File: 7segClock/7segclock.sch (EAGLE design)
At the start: 19 parts, among them J1 ICSP, J2 ZX62R-AB-5P, Q1 CSTNE16M0V530000R0, U1 ATMEGA328P-AU-TQFP32, U2 TM1640, U3 CP2104

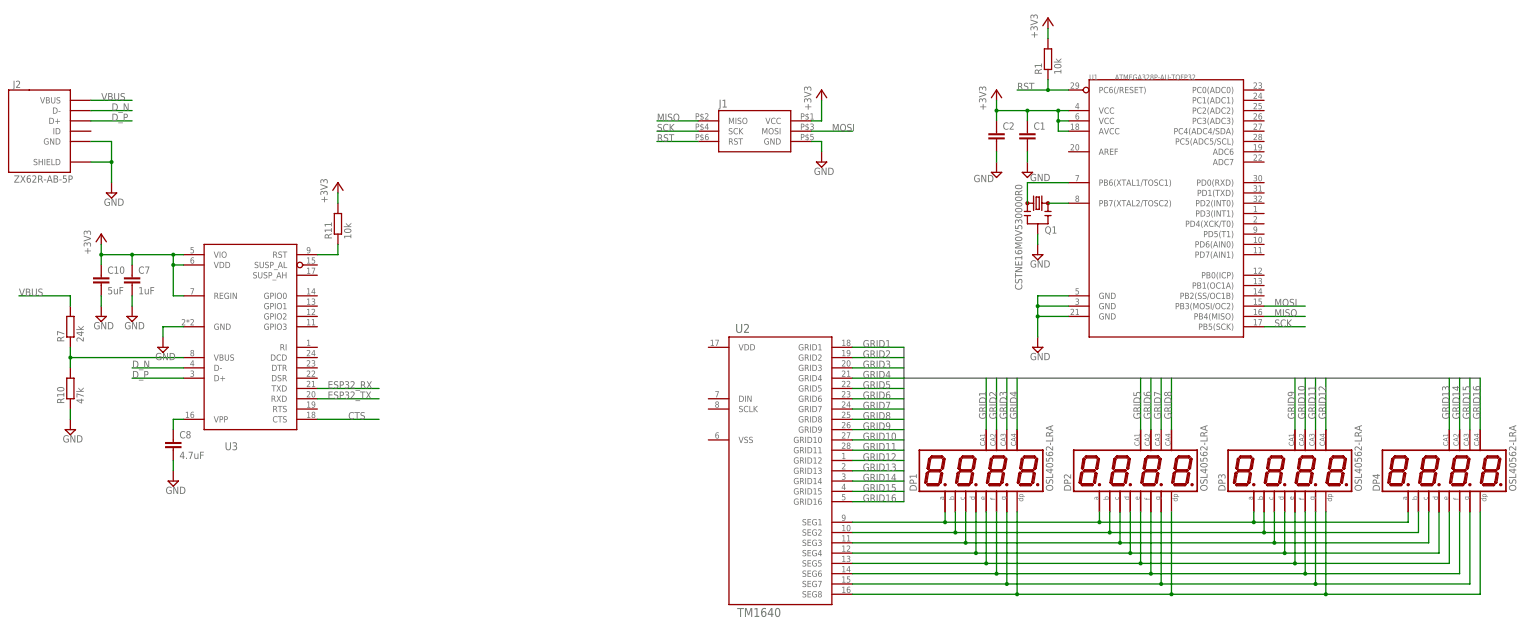
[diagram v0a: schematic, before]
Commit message: [add]add 7seg clokc before autoroute
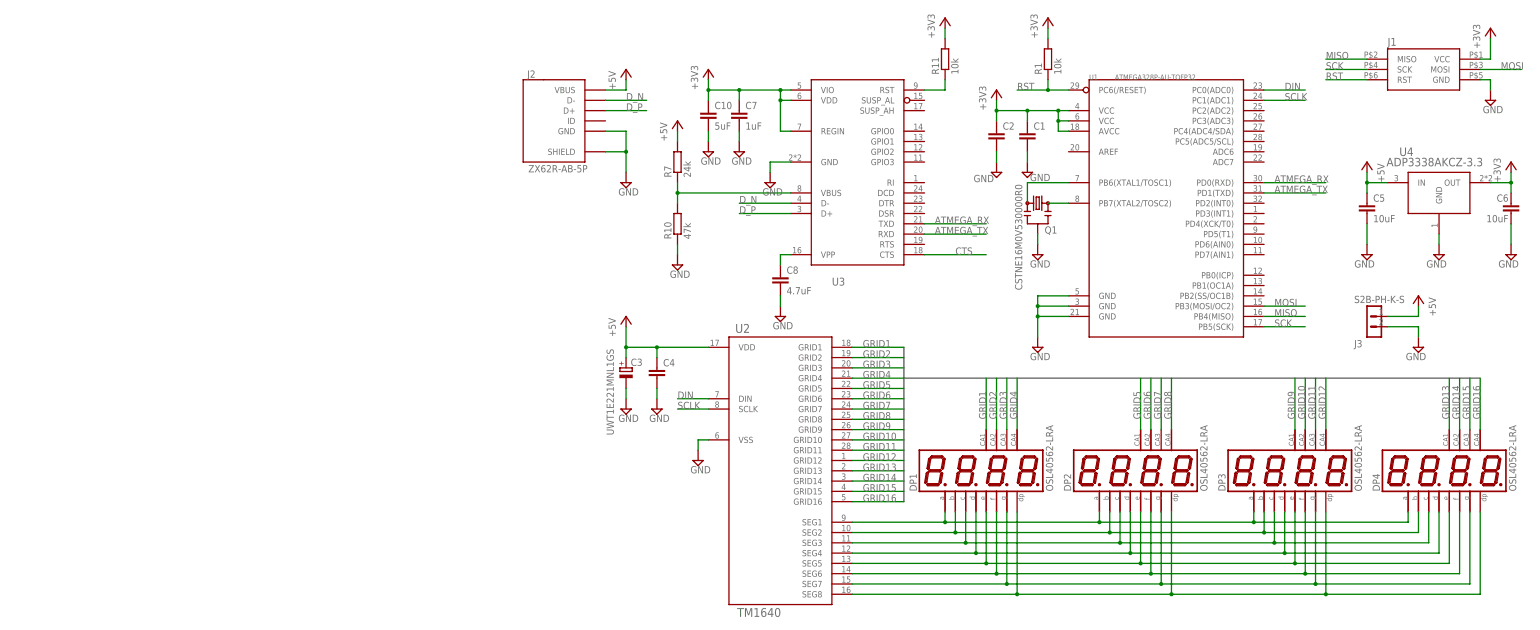
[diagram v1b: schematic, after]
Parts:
- added C3: UWT1E221MNL1GS, taki-library:UWT1E221MNL1GS
- added C4: (no value), taki-library:C-EUC0603
- added C5, C6: 10uF, taki-library:C-EUC0603
- added J3: S2B-PH-K-S, taki-library:S2B-PH-K-S
- added U4: ADP3338AKCZ-3.3, taki-library:ADP3338AKCZ-3.3
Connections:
- removed net ESP32_RX: U3.TXD
- removed net ESP32_TX: U3.RXD
- removed net VBUS: J2.VBUS, R7.2
- new net +5V: C3.+, C4.1, C5.1, J2.VBUS, J3.1, R7.2, U2.VDD, U4.IN
- new net ATMEGA_RX: U1.PD0(RXD), U3.TXD
- new net ATMEGA_TX: U1.PD1(TXD), U3.RXD
- new net DIN: U1.PC0(ADC0), U2.DIN
- new net SCLK: U1.PC1(ADC1), U2.SCLK
- net +3V3: now also C6.1, U4.OUT
- net GND: now also C3.-, C4.2, C5.2, C6.2, J3.2, U2.VSS, U4.GND
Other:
- moved on the sheet: C10, C7, C8, J1, J2, R10, R11, R7, U3

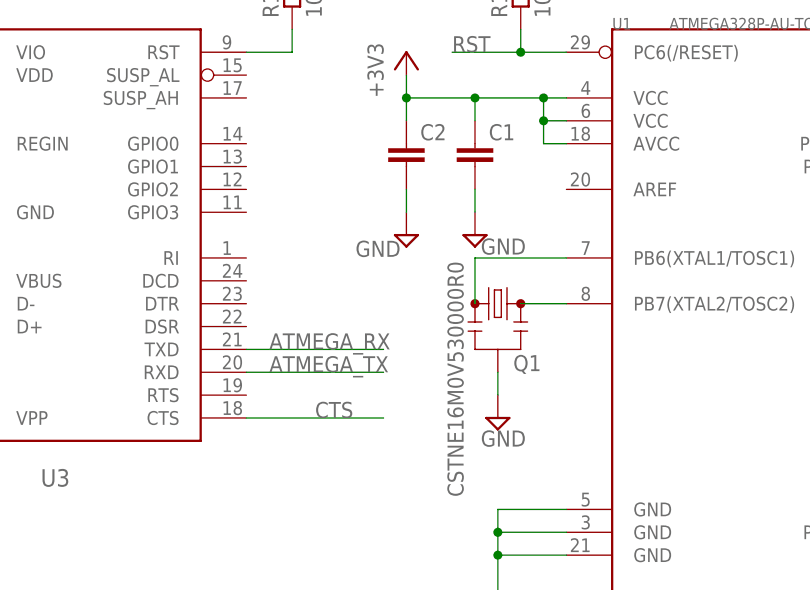
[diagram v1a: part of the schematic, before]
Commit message: [add]add gerver output of 7seg clokc
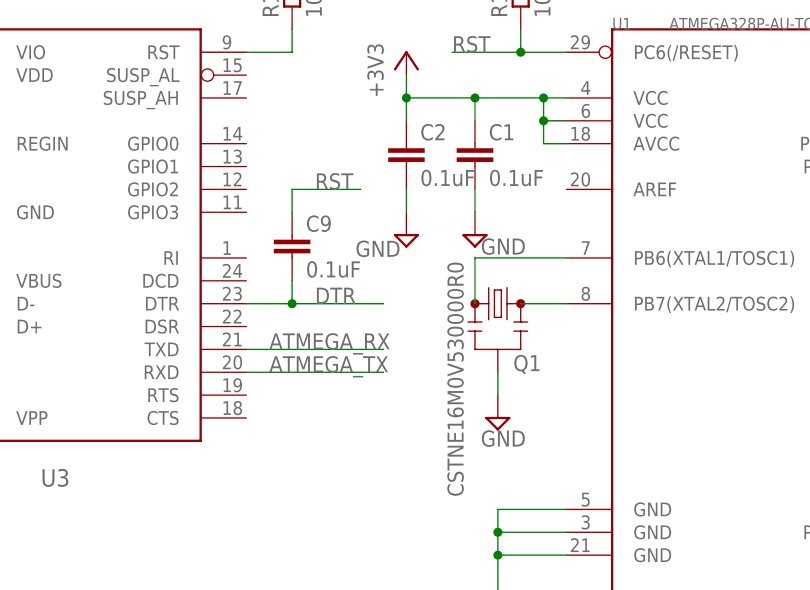
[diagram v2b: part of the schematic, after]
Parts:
- added C9: 0.1uF, taki-library:C-EUC0603
- C1, C2: value (none) -> 0.1uF
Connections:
- removed net CTS: U3.CTS
- new net DTR: C9.2, U3.DTR
- net RST: now also C9.1
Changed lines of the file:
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@@
 </variantdefs>
 <classes>
-<class number="0" name="default" width="0.1524" drill="0">
+<class number="0" name="default" width="0.0051625" drill="0">
 </class>
 <class number="1" name="POWER" width="0.254" drill="0">
@@
 <part name="SUPPLY1" library="taki-library" deviceset="GND" device=""/>
 <part name="U2" library="taki-library" deviceset="TM1640" device=""/>
-<part name="C1" library="taki-library" deviceset="C-EU" device="C0603"/>
-<part name="C2" library="taki-library" deviceset="C-EU" device="C0603"/>
+<part name="C1" library="taki-library" deviceset="C-EU" device="C0603" value="0.1uF"/>
+<part name="C2" library="taki-library" deviceset="C-EU" device="C0603" value="0.1uF"/>
 <part name="SUPPLY2" library="taki-library" deviceset="GND" device=""/>
 <part name="SUPPLY3" library="taki-library" deviceset="GND" device=""/>
@@
 <part name="SUPPLY16" library="taki-library" deviceset="GND" device=""/>
 <part name="P+5" library="taki-library" deviceset="+5V" device=""/>
+<part name="C9" library="taki-library" deviceset="C-EU" device="C0603" value="0.1uF"/>
 </parts>
 <sheets>
@@
 <instance part="P+5" gate="1" x="228.6" y="104.14" smashed="yes" rot="MR0">
 <attribute name="VALUE" x="231.14" y="99.06" size="1.778" layer="96" rot="MR90"/>
+</instance>
+<instance part="C9" gate="G$1" x="111.76" y="134.62" smashed="yes">
+<attribute name="NAME" x="113.284" y="135.001" size="1.778" layer="95"/>
+<attribute name="VALUE" x="113.284" y="129.921" size="1.778" layer="96"/>
 </instance>
 </instances>
@@
 <wire x1="215.9" y1="157.48" x2="205.74" y2="157.48" width="0.1524" layer="91"/>
 <label x="205.74" y="157.48" size="1.778" layer="95"/>
+</segment>
+<segment>
+<wire x1="119.38" y1="139.7" x2="111.76" y2="139.7" width="0.1524" layer="91"/>
+<pinref part="C9" gate="G$1" pin="1"/>
+<wire x1="111.76" y1="137.16" x2="111.76" y2="139.7" width="0.1524" layer="91"/>
+<label x="114.3" y="139.7" size="1.778" layer="95"/>
 </segment>
 </net>
@@
 </segment>
 </net>
-<net name="CTS" class="0">
-<segment>
-<pinref part="U3" gate="G$1" pin="CTS"/>
-<wire x1="106.68" y1="114.3" x2="121.92" y2="114.3" width="0.1524" layer="91"/>
-<label x="114.3" y="114.3" size="1.778" layer="95"/>
-</segment>
-</net>
 <net name="DIN" class="0">
 <segment>
@@
 </segment>
 </net>
+<net name="DTR" class="0">
+<segment>
+<pinref part="U3" gate="G$1" pin="DTR"/>
+<wire x1="106.68" y1="127" x2="111.76" y2="127" width="0.1524" layer="91"/>
+<label x="114.3" y="127" size="1.778" layer="95"/>
+<pinref part="C9" gate="G$1" pin="2"/>
+<wire x1="111.76" y1="127" x2="121.92" y2="127" width="0.1524" layer="91"/>
+<wire x1="111.76" y1="127" x2="111.76" y2="129.54" width="0.1524" layer="91"/>
+<junction x="111.76" y="127"/>
+</segment>
+</net>
